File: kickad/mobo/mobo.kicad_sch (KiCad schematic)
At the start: 18 parts, among them J1 nice!view, J10 rgb, J11 rows, J12 columns, J13 columns, J2 Battery, J4 rotary, J5 trackball, J6 nice!view, J7 Battery, J8 rgb, J9 rows, SW1 Power, SW2 Reset, SW3 Reset, SW4 Power, U1 nice!nano v2, U3 nice!nano v2

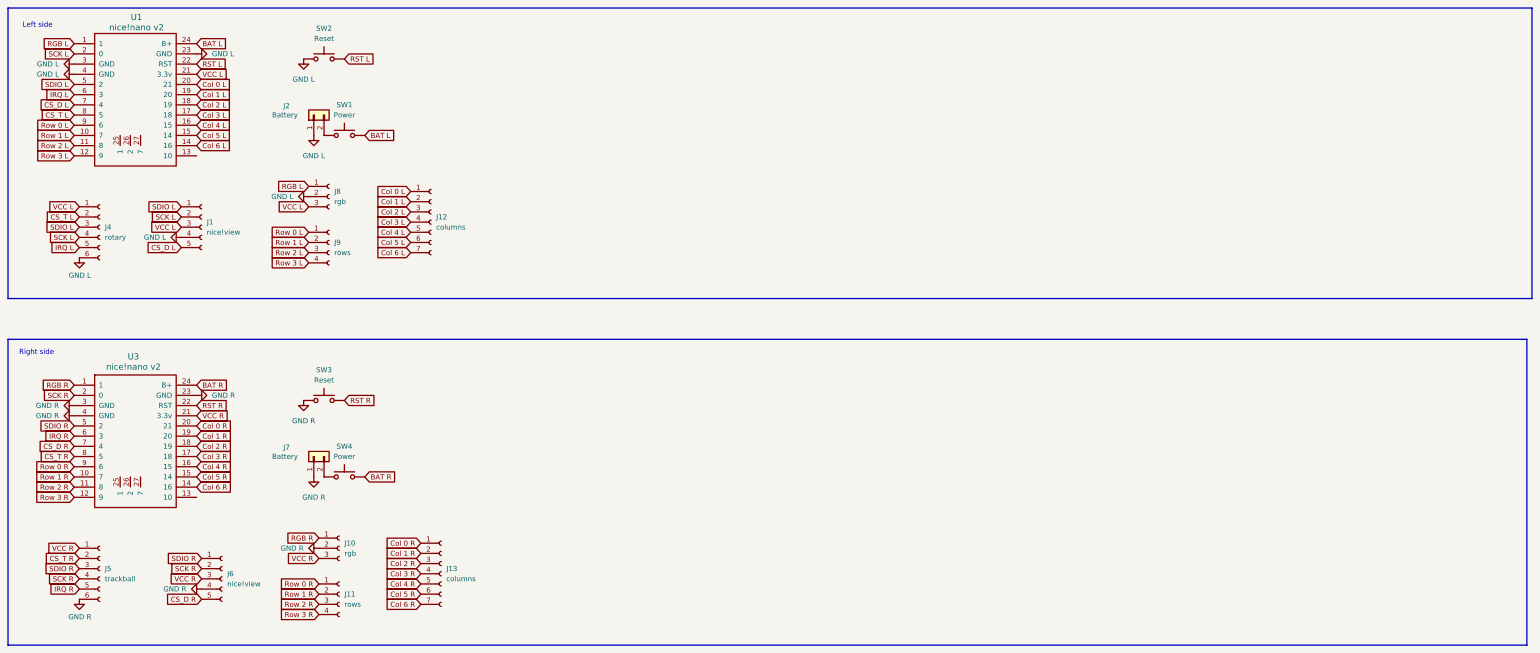
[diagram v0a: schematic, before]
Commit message: Resetting the mobo stack to 4 layers mirrorable
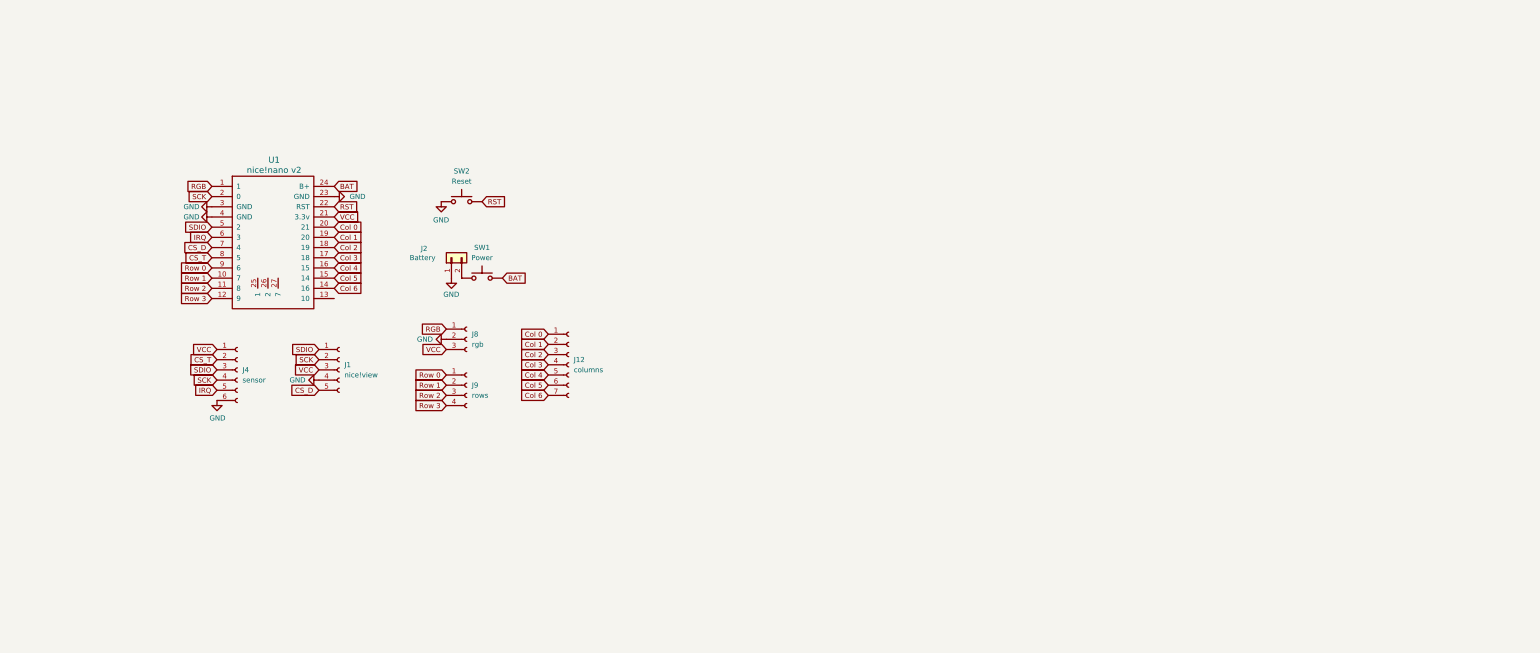
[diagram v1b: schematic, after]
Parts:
- removed J10: rgb, Connector_Wuerth:Wuerth_WR-WTB_64800311622_1x03_P1.50mm_Vertical, symbol Connector:Conn_01x03_Socket
- removed J11: rows, Connector_Wuerth:Wuerth_WR-WTB_64800411622_1x04_P1.50mm_Vertical, symbol Connector:Conn_01x04_Socket
- removed J13: columns, Connector_Wuerth:Wuerth_WR-WTB_64800711622_1x07_P1.50mm_Vertical, symbol Connector:Conn_01x07_Socket
- removed J5: trackball, Connector_Wuerth:Wuerth_WR-WTB_64800611622_1x06_P1.50mm_Vertical, symbol Connector:Conn_01x06_Socket
- removed J6: nice!view, Connector_PinHeader_2.54mm:PinHeader_1x05_P2.54mm_Vertical, symbol Connector:Conn_01x05_Socket
- removed J7: Battery, Connector_JST:JST_ZH_S2B-ZR-SM4A-TF_1x02-1MP_P1.50mm_Horizontal, symbol Connector_Generic:Conn_01x02
- removed SW3: Reset, Button_Switch_SMD:SW_SPST_B3U-1000P, symbol ScottoKeebs:Placeholder_Switch
- removed SW4: Power, Button_Switch_SMD:SW_SPDT_PCM12, symbol ScottoKeebs:Placeholder_Switch
- removed U3: nice!nano v2, ScottoKeebs_MCU:Nice_Nano_V2_Flipped, symbol ScottoKeebs:MCU_Nice_Nano_V2
- J4: value rotary -> sensor
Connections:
- net BAT L renamed BAT
- net CS_D L renamed CS_D
- net CS_T L renamed CS_T
- net Col 0 L renamed Col 0
- net Col 1 L renamed Col 1
- net Col 2 L renamed Col 2
- net Col 3 L renamed Col 3
- net Col 4 L renamed Col 4
- net Col 5 L renamed Col 5
- net Col 6 L renamed Col 6
- net GND L renamed GND
- net IRQ L renamed IRQ
- net RGB L renamed RGB
- net RST L renamed RST
- net Row 0 L renamed Row 0
- net Row 1 L renamed Row 1
- net Row 2 L renamed Row 2
- net Row 3 L renamed Row 3
- net SCK L renamed SCK
- net SDIO L renamed SDIO
- net VCC L renamed VCC
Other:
- note removed: "Left side"
- note removed: "Right side"
- moved on the sheet: J1, J12, J2, J4, J8, J9, SW1, SW2, U1
